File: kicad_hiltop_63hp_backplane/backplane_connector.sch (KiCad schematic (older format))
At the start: 49 parts, among them J15 CONN_DIN_HDR_96POS, J16 CONN_DIN_HDR_96POS, J17 CONN_DIN_HDR_96POS, U2 LTC4311, U3 LTC4311

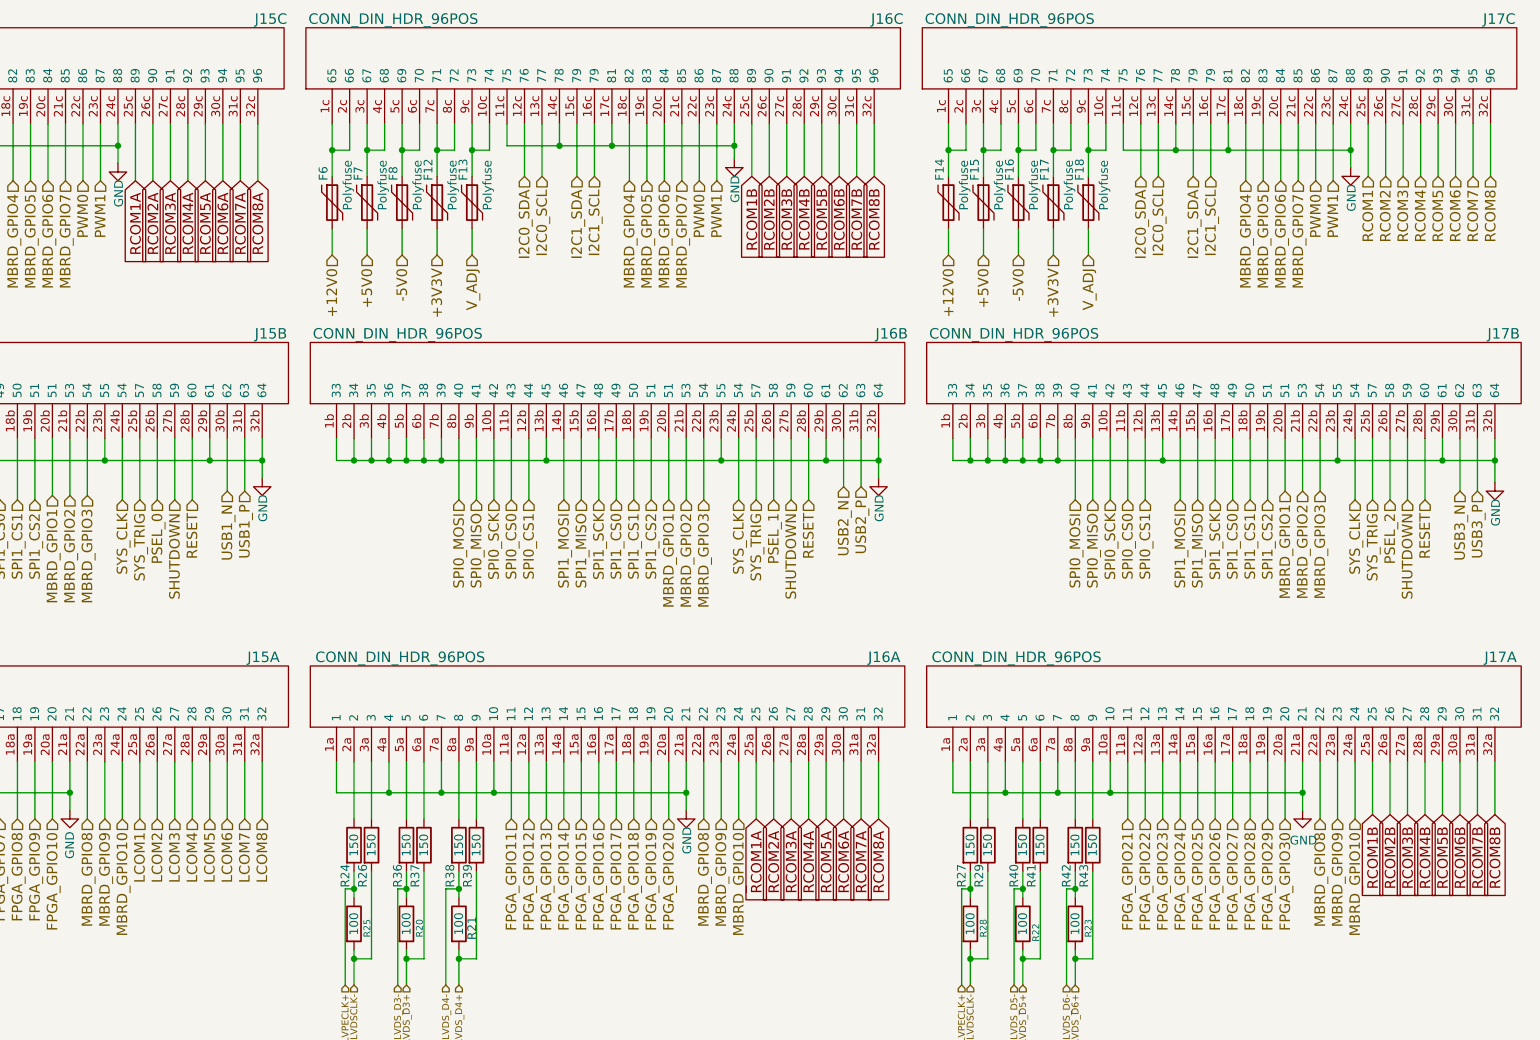
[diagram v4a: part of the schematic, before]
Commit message: Schematic updated to reflect USB logic and Global nets changed to local nets, renamed signals in motherboard connector
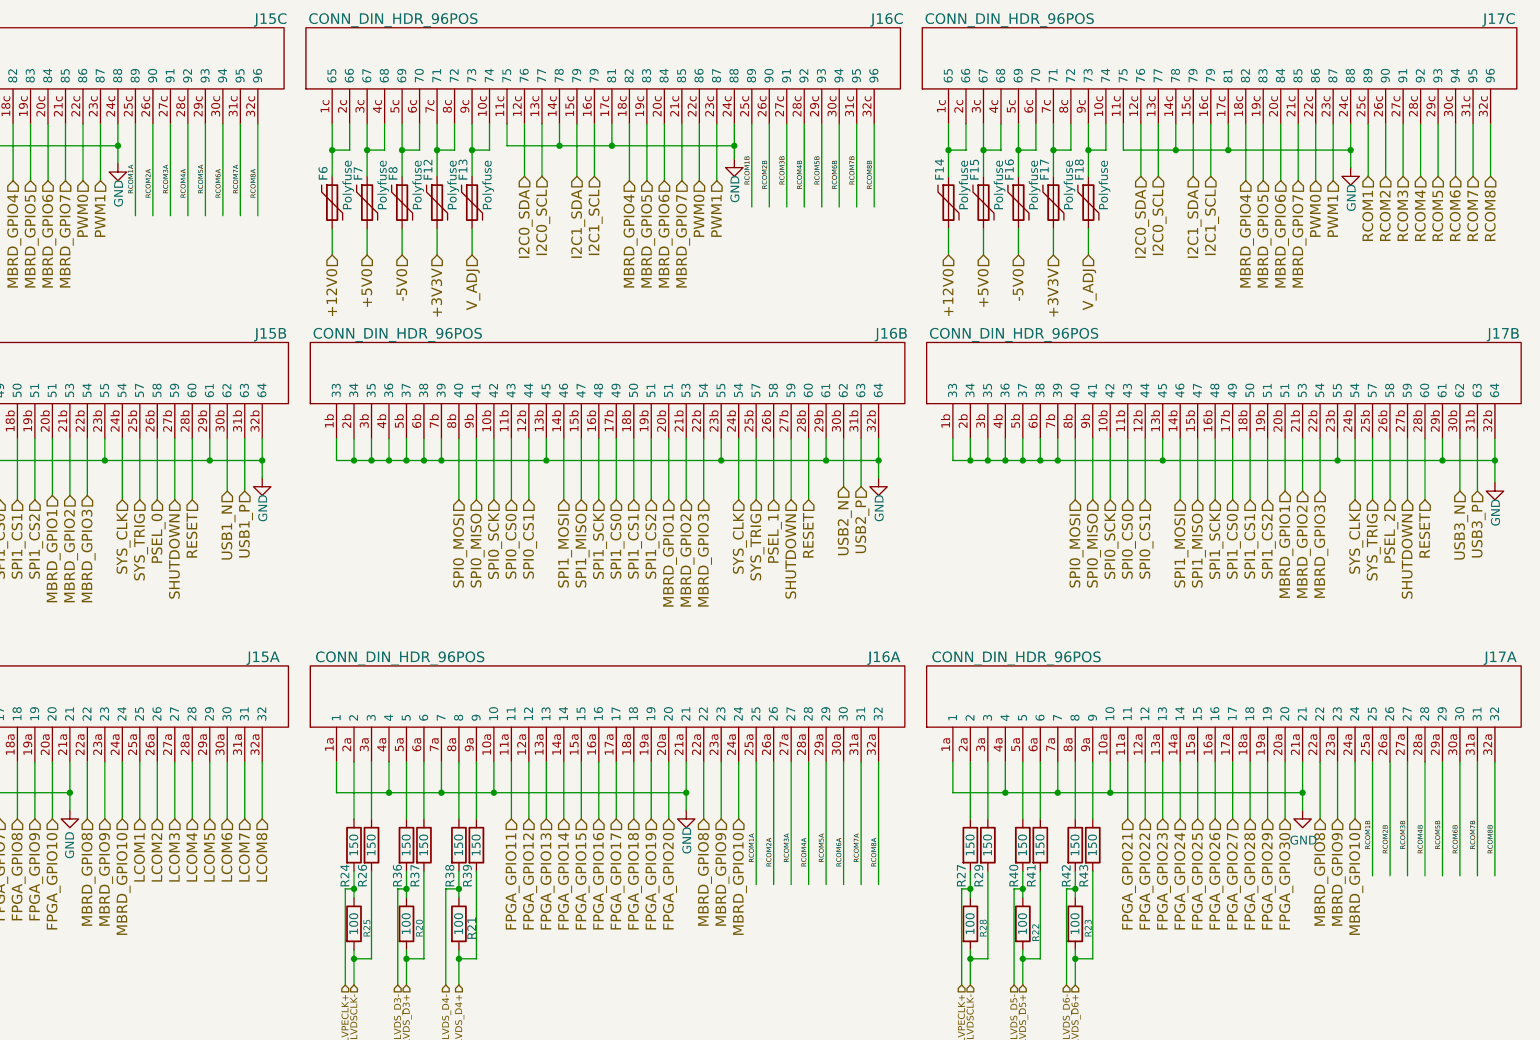
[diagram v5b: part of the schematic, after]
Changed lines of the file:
@@
 $Descr A4 11693 8268
 encoding utf-8
-Sheet 4 6
+Sheet 3 6
 Title ""
 Date ""
@@
 	3900 4825 3900 5150
 Wire Wire Line
-	3175 1175 3175 1500
-Wire Wire Line
-	3275 1175 3275 1500
-Wire Wire Line
-	3375 1175 3375 1500
-Wire Wire Line
-	3475 1175 3475 1500
-Wire Wire Line
-	3575 1500 3575 1175
-Wire Wire Line
-	3675 1500 3675 1175
-Wire Wire Line
-	3775 1500 3775 1175
-Wire Wire Line
-	3875 1500 3875 1175
-Wire Wire Line
-	6725 4825 6725 5150
-Wire Wire Line
-	6825 4825 6825 5150
-Wire Wire Line
-	6925 4825 6925 5150
-Wire Wire Line
-	7025 4825 7025 5150
-Wire Wire Line
-	7125 5150 7125 4825
-Wire Wire Line
-	7225 5150 7225 4825
-Wire Wire Line
-	7325 5150 7325 4825
-Wire Wire Line
-	7425 5150 7425 4825
-Wire Wire Line
-	6700 1175 6700 1475
-Wire Wire Line
-	6900 1175 6900 1475
-Wire Wire Line
-	7000 1175 7000 1475
-Wire Wire Line
-	7100 1175 7100 1475
-Wire Wire Line
-	7200 1175 7200 1475
-Wire Wire Line
-	7300 1175 7300 1475
-Wire Wire Line
-	7400 1175 7400 1475
-Text GLabel 6700 1475 3    60   Input ~ 0
-RCOM1B
-Wire Wire Line
-	6800 1175 6800 1475
-Text GLabel 6800 1475 3    60   Input ~ 0
-RCOM2B
-Text GLabel 6900 1475 3    60   Input ~ 0
-RCOM3B
-Text GLabel 7000 1475 3    60   Input ~ 0
-RCOM4B
-Text GLabel 7100 1475 3    60   Input ~ 0
-RCOM5B
-Text GLabel 7200 1475 3    60   Input ~ 0
-RCOM6B
-Text GLabel 7300 1475 3    60   Input ~ 0
-RCOM7B
-Text GLabel 7400 1475 3    60   Input ~ 0
-RCOM8B
-Wire Wire Line
-	10250 4825 10250 5125
-Wire Wire Line
-	10450 4825 10450 5125
-Wire Wire Line
-	10550 4825 10550 5125
-Wire Wire Line
-	10650 4825 10650 5125
-Wire Wire Line
-	10750 4825 10750 5125
-Wire Wire Line
-	10850 4825 10850 5125
-Wire Wire Line
-	10950 4825 10950 5125
-Wire Wire Line
-	10350 4825 10350 5125
+	3175 1175 3175 1700
+Wire Wire Line
+	3275 1175 3275 1700
+Wire Wire Line
+	3375 1175 3375 1700
+Wire Wire Line
+	3475 1175 3475 1700
+Wire Wire Line
+	3575 1700 3575 1175
+Wire Wire Line
+	3675 1700 3675 1175
+Wire Wire Line
+	3775 1700 3775 1175
+Wire Wire Line
+	3875 1700 3875 1175
+Wire Wire Line
+	6725 4825 6725 5525
+Wire Wire Line
+	6825 4825 6825 5525
+Wire Wire Line
+	6925 4825 6925 5525
+Wire Wire Line
+	7025 4825 7025 5525
+Wire Wire Line
+	7125 5525 7125 4825
+Wire Wire Line
+	7225 5525 7225 4825
+Wire Wire Line
+	7325 5525 7325 4825
+Wire Wire Line
+	7425 5525 7425 4825
+Wire Wire Line
+	6700 1175 6700 1650
+Wire Wire Line
+	6900 1175 6900 1650
+Wire Wire Line
+	7000 1175 7000 1650
+Wire Wire Line
+	7100 1175 7100 1650
+Wire Wire Line
+	7200 1175 7200 1650
+Wire Wire Line
+	7300 1175 7300 1650
+Wire Wire Line
+	7400 1175 7400 1650
+Wire Wire Line
+	6800 1175 6800 1650
+Wire Wire Line
+	10250 4825 10250 5475
+Wire Wire Line
+	10450 4825 10450 5475
+Wire Wire Line
+	10550 4825 10550 5475
+Wire Wire Line
+	10650 4825 10650 5475
+Wire Wire Line
+	10750 4825 10750 5475
+Wire Wire Line
+	10850 4825 10850 5475
+Wire Wire Line
+	10950 4825 10950 5475
+Wire Wire Line
+	10350 4825 10350 5475
 Wire Wire Line
 	10225 1175 10225 1475
@@
 Text HLabel 10225 1475 3    60   Input ~ 0
 RCOM1
-Text GLabel 3175 1500 3    60   Input ~ 0
-RCOM1A
-Text GLabel 3275 1500 3    60   Input ~ 0
-RCOM2A
-Text GLabel 3375 1500 3    60   Input ~ 0
-RCOM3A
-Text GLabel 3475 1500 3    60   Input ~ 0
-RCOM4A
-Text GLabel 3575 1500 3    60   Input ~ 0
-RCOM5A
-Text GLabel 3675 1500 3    60   Input ~ 0
-RCOM6A
-Text GLabel 3775 1500 3    60   Input ~ 0
-RCOM7A
-Text GLabel 3875 1500 3    60   Input ~ 0
-RCOM8A
-Text GLabel 6725 5150 3    60   Input ~ 0
-RCOM1A
-Text GLabel 6825 5150 3    60   Input ~ 0
-RCOM2A
-Text GLabel 6925 5150 3    60   Input ~ 0
-RCOM3A
-Text GLabel 7025 5150 3    60   Input ~ 0
-RCOM4A
-Text GLabel 7125 5150 3    60   Input ~ 0
-RCOM5A
-Text GLabel 7225 5150 3    60   Input ~ 0
-RCOM6A
-Text GLabel 7325 5150 3    60   Input ~ 0
-RCOM7A
-Text GLabel 7425 5150 3    60   Input ~ 0
-RCOM8A
-Text GLabel 10250 5125 3    60   Input ~ 0
-RCOM1B
-Text GLabel 10350 5125 3    60   Input ~ 0
-RCOM2B
-Text GLabel 10450 5125 3    60   Input ~ 0
-RCOM3B
-Text GLabel 10550 5125 3    60   Input ~ 0
-RCOM4B
-Text GLabel 10650 5125 3    60   Input ~ 0
-RCOM5B
-Text GLabel 10750 5125 3    60   Input ~ 0
-RCOM6B
-Text GLabel 10850 5125 3    60   Input ~ 0
-RCOM7B
-Text GLabel 10950 5125 3    60   Input ~ 0
-RCOM8B
 Text HLabel 10325 1475 3    60   Input ~ 0
 RCOM2
@@
 Text HLabel 1000 6950 0    39   Input ~ 0
 +3V3
+Text Label 3175 1575 1    28   ~ 0
+RCOM1A
+Text Label 3275 1600 1    28   ~ 0
+RCOM2A
+Text Label 3375 1575 1    28   ~ 0
+RCOM3A
+Text Label 3475 1600 1    28   ~ 0
+RCOM4A
+Text Label 3575 1575 1    28   ~ 0
+RCOM5A
+Text Label 3675 1600 1    28   ~ 0
+RCOM6A
+Text Label 3775 1575 1    28   ~ 0
+RCOM7A
+Text Label 3875 1600 1    28   ~ 0
+RCOM8A
+Text Label 6700 1525 1    28   ~ 0
+RCOM1B
+Text Label 6800 1550 1    28   ~ 0
+RCOM2B
+Text Label 6900 1525 1    28   ~ 0
+RCOM3B
+Text Label 7000 1550 1    28   ~ 0
+RCOM4B
+Text Label 7100 1525 1    28   ~ 0
+RCOM5B
+Text Label 7200 1550 1    28   ~ 0
+RCOM6B
+Text Label 7300 1525 1    28   ~ 0
+RCOM7B
+Text Label 7400 1550 1    28   ~ 0
+RCOM8B
+Text Label 10250 5325 1    28   ~ 0
+RCOM1B
+Text Label 10350 5350 1    28   ~ 0
+RCOM2B
+Text Label 10450 5325 1    28   ~ 0
+RCOM3B
+Text Label 10550 5350 1    28   ~ 0
+RCOM4B
+Text Label 10650 5325 1    28   ~ 0
+RCOM5B
+Text Label 10750 5350 1    28   ~ 0
+RCOM6B
+Text Label 10850 5325 1    28   ~ 0
+RCOM7B
+Text Label 10950 5350 1    28   ~ 0
+RCOM8B
+Text Label 6725 5400 1    28   ~ 0
+RCOM1A
+Text Label 6825 5425 1    28   ~ 0
+RCOM2A
+Text Label 6925 5400 1    28   ~ 0
+RCOM3A
+Text Label 7025 5425 1    28   ~ 0
+RCOM4A
+Text Label 7125 5400 1    28   ~ 0
+RCOM5A
+Text Label 7225 5425 1    28   ~ 0
+RCOM6A
+Text Label 7325 5400 1    28   ~ 0
+RCOM7A
+Text Label 7425 5425 1    28   ~ 0
+RCOM8A
 $EndSCHEMATC

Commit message: lables connected to end of net, each component mapped to footprint, working on reducing error
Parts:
- F1, F2, F3, F6, F7, F8: value Polyfuse -> 1206L050; footprint (none) -> Fuse:Fuse_1206_3216Metric
- F10: renamed from F13; value Polyfuse -> 2920L100PR; footprint (none) -> Fuse:Fuse_2920_7451Metric
- F11: renamed from F14; value Polyfuse -> 1206L050; footprint (none) -> Fuse:Fuse_1206_3216Metric
- F12: renamed from F15; value Polyfuse -> 1206L050; footprint (none) -> Fuse:Fuse_1206_3216Metric
- F13: renamed from F16; value Polyfuse -> 1206L050; footprint (none) -> Fuse:Fuse_1206_3216Metric
- F14: renamed from F17; value Polyfuse -> 1206L075; footprint (none) -> Fuse:Fuse_1206_3216Metric
- F15: renamed from F18; value Polyfuse -> 2920L100PR; footprint (none) -> Fuse:Fuse_2920_7451Metric
- F4: value Polyfuse -> 1206L075; footprint (none) -> Fuse:Fuse_1206_3216Metric
- F5: value Polyfuse -> 2920L100PR; footprint (none) -> Fuse:Fuse_2920_7451Metric
- F9: renamed from F12; value Polyfuse -> 1206L075; footprint (none) -> Fuse:Fuse_1206_3216Metric
- J4: renamed from J15; footprint (none) -> Connectors_IEC_DIN:Socket_DIN41612-CaseC1-full-Male-96Pin-3rows
- J5: renamed from J16; footprint (none) -> Connectors_IEC_DIN:Socket_DIN41612-CaseC1-full-Male-96Pin-3rows
- J6: renamed from J17; footprint (none) -> Connectors_IEC_DIN:Socket_DIN41612-CaseC1-full-Male-96Pin-3rows
- renumbered C19 to C20, C20 to C21, R56 to R18, R30 to R19, R57 to R20, R32 to R21, R18 to R22, R33 to R23, R34 to R24, R19 to R25, R35 to R26, R24 to R27, R25 to R28, R26 to R29, R36 to R30, R20 to R31, R37 to R32, R38 to R33, R21 to R34, R39 to R35, R27 to R36, R28 to R37, R29 to R38, R40 to R39, R22 to R40, R23 to R43, R43 to R44, U2 to U3, U3 to U4
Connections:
- net labels removed: +3V3V
- wire segments 491 -> 493
- no-connect marks 0 -> 2
